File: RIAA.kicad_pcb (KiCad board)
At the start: 2 copper layers, 112 x 202 mm, 44 parts, among them K1 G6K-2, P1 Fra Hovedprint, P2 Fra Ledning, U1 OPA2134, U2 LM317_TO-220

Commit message: feat: reversed D1.
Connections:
- D1 pad 1: 24VDC+ -> 30V
- D1 pad 2: 30V -> 24VDC+
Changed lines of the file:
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@@
 			(layers "*.Cu" "*.Mask")
 			(remove_unused_layers no)
-			(net 14 "24VDC+")
+			(net 15 "30V")
 			(pinfunction "K")
 			(pintype "passive")
@@
 			(layers "*.Cu" "*.Mask")
 			(remove_unused_layers no)
-			(net 15 "30V")
+			(net 14 "24VDC+")
 			(pinfunction "A")
 			(pintype "passive")

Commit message: feat: Updated PSU resistor values.
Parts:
- R1: value 4370 -> 5k6
- R2: value 240 -> 300
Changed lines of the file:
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@@
 			)
 		)
-		(property "Value" "4370"
+		(property "Value" "5k6"
 			(at 3.81 1.92 0)
 			(layer "F.Fab")
@@
 			)
 		)
-		(property "Value" "240"
+		(property "Value" "300"
 			(at 3.81 1.92 0)
 			(layer "F.Fab")

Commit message: feat: Updated PCB.
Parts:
- moved C6 83.7 mm to (165.0, 110.7)
- moved U2 68.7 mm to (150.3, 127.0), turned to -90 degrees
- moved R2 66.8 mm to (183.4, 105.4), turned to 180 degrees
- moved R1 60.3 mm to (163.7, 120.8)
- moved R7 58.7 mm to (239.4, 187.3), turned to 180 degrees
- moved R8 54.4 mm to (231.8, 190.5)
- moved R4 53.3 mm to (231.8, 173.4)
- moved C9 52.5 mm to (180.9, 143.4), turned to 90 degrees
- moved C4 51.9 mm to (218.2, 130.3)
- moved R6 50.6 mm to (231.8, 179.7)
- moved R5 50.6 mm to (231.8, 176.5)
- moved C3 48.9 mm to (149.3, 111.1)
- moved D2 47.5 mm to (188.4, 111.0), turned to 180 degrees
- moved D1 46.1 mm to (173.2, 134.6), turned to 90 degrees
- moved R11 37.1 mm to (205.3, 168.2), turned to 180 degrees
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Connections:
- R11 pad 2: Net-(R11-Pad2) -> GND
- R13 pad 2: Net-(R11-Pad2) -> GND
- R3 pad 2: Net-(R3-Pad2) -> GND
- R5 pad 2: Net-(R3-Pad2) -> GND
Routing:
- net 24VDC+: track 0.00 -> 151.4 mm
- net 24VDC-: track 0.00 -> 54.6 mm
- net 30V: track 7.53 -> 58.6 mm
- net Net-(D2-A): track 0.00 -> 46.1 mm
- net Net-(C11-Pad1): track 0.00 -> 25.2 mm
- net Net-(C16-Pad1): track 0.00 -> 25.1 mm
- net Net-(C10-Pad1): track 0.00 -> 16.7 mm
- net Net-(C15-Pad1): track 0.00 -> 15.9 mm
- net GND: track 78.3 -> 90.4 mm
- net Net-(C15-Pad2): track 0.00 -> 10.7 mm
- net Net-(U3B-+): track 0.00 -> 9.72 mm
- net Net-(U3A-+): track 0.00 -> 8.94 mm
- net Net-(C10-Pad2): track 0.00 -> 8.87 mm
- net R IN  PICKUP: track 0.00 -> 5.52 mm
- net L IN  PICKUP: track 0.00 -> 5.05 mm
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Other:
- board text removed: "PSU"

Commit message: WIP
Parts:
- removed U1: OPA2134, Package_SO:SOIC-8_3.9x4.9mm_P1.27mm
- added U3: OPA2134, OPA2134:D8, F.Cu at (199.0, 181.0)
- moved C10 21.5 mm to (219.9, 189.0)
- moved C11 21.5 mm to (211.0, 189.0)
- moved C12 21.5 mm to (213.6, 199.8)
- moved C16 21.5 mm to (184.9, 187.5)
- moved R15 21.5 mm to (177.0, 191.9)
- moved R3 21.5 mm to (211.0, 175.7)
- moved R4 21.5 mm to (211.0, 178.9)
- moved R5 21.5 mm to (211.0, 182.1)
- moved R7 21.5 mm to (218.6, 192.8)
- moved R8 21.5 mm to (211.0, 196.0)
- moved C15 21.5 mm to (175.8, 187.6)
- moved C17 21.5 mm to (182.0, 200.4)
- moved C8 21.5 mm to (216.1, 171.3)
- moved R6 21.5 mm to (211.0, 185.2)
- moved C14 21.5 mm to (179.7, 169.6)
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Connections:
- BC1 pad 3: 24VDC- -> GND
- C14 pad 2: L IN  PICKUP -> L IN PICKUP
- C3 pad 2: 24VDC- -> GND
- C4 pad 1: 24VDC- -> Net-(U3C-V-)
- C5 pad 2: 24VDC- -> Net-(U3C-V-)
- C6 pad 2: 24VDC- -> GND
- C7 pad 2: 24VDC- -> GND
- C8 pad 2: R IN  PICKUP -> R IN PICKUP
- C9 pad 1: 24VDC- -> GND
- P1 pad 2: 24VDC- -> GND
- P1 pad 3: 24VDC- -> GND
- P2 pad 6: 24VDC- -> GND
- R1 pad 2: 24VDC- -> GND
- R11 pad 1: L IN  PICKUP -> L IN PICKUP
- R3 pad 1: R IN  PICKUP -> R IN PICKUP
- R9 pad 1: 24VDC- -> GND
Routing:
- net 24VDC-: track 54.6 -> 0.00 mm
- net 30V: track 58.6 -> 89.8 mm
- net GND: track 90.4 -> 66.7 mm
- net Net-(BC1-C): track 26.2 -> 40.8 mm, vias 0 -> 2
- net R OUT: track 17.0 -> 5.29 mm
- net 21V: track 45.9 -> 57.0 mm
- net R IN PICKUP: track 0.00 -> 5.52 mm
- net R IN  PICKUP: track 5.52 -> 0.00 mm
- net L IN PICKUP: track 0.00 -> 5.05 mm
- net L IN  PICKUP: track 5.05 -> 0.00 mm
- net L OUT: track 8.73 -> 4.35 mm
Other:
- board text added: "MUTE RELAY"
- board text added: "POWER"
- board text added: "RIAA"

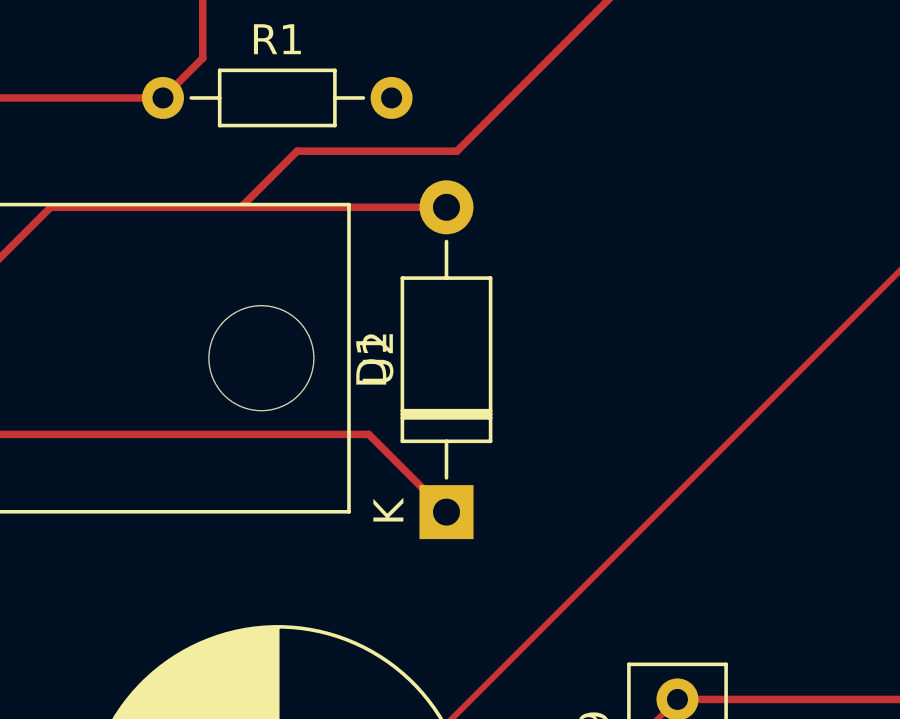
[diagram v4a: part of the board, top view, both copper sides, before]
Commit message: feat: Updated orientation of D1.
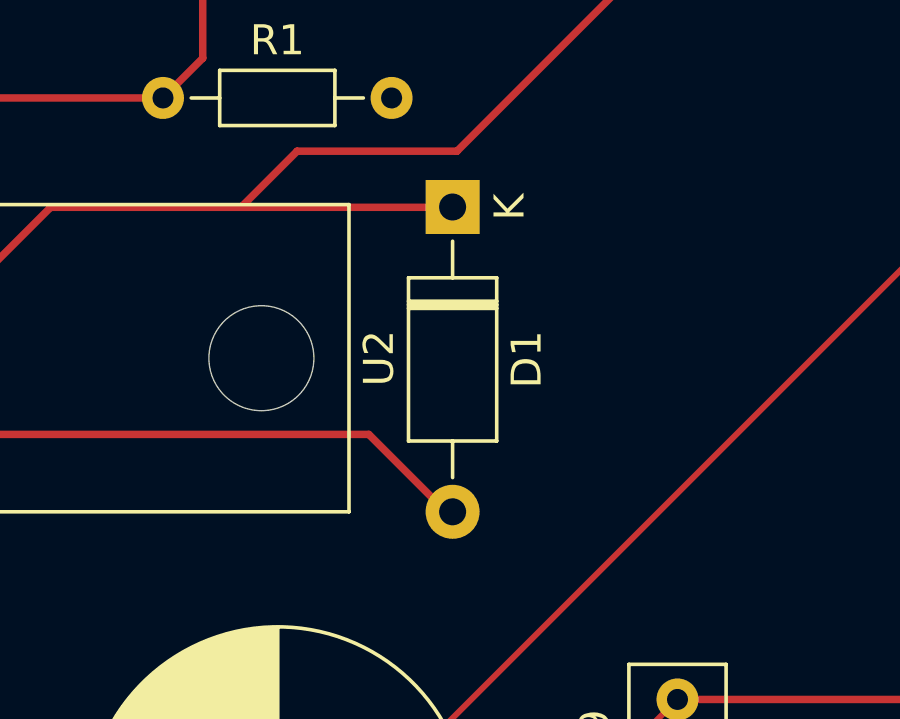
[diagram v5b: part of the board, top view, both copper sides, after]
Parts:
- moved D1 10.2 mm to (173.4, 124.5), turned to -90 degrees
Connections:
- D1 pad 1: 30V -> 24VDC+
- D1 pad 2: 24VDC+ -> 30V
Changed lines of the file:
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@@
 	(footprint "Diode_THT:D_A-405_P10.16mm_Horizontal"
 		(layer "F.Cu")
-		(at 173.151041 134.63 90)
+		(at 173.355 124.46 -90)
 		(descr "Diode, A-405 series, Axial, Horizontal, pin pitch=10.16mm, , length*diameter=5.2*2.7mm^2, , http://www.diodes.com/_files/packages/A-405.pdf")
 		(tags "Diode A-405 series Axial Horizontal pin pitch 10.16mm  length 5.2mm diameter 2.7mm")
@@
 		)
 		(property "Footprint" "Diode_THT:D_A-405_P10.16mm_Horizontal"
-			(at 0 0 90)
+			(at 0 0 -90)
 			(unlocked yes)
 			(layer "F.Fab")
@@
 		)
 		(property "Datasheet" ""
-			(at 0 0 90)
+			(at 0 0 -90)
 			(unlocked yes)
 			(layer "F.Fab")
@@
 		)
 		(property "Description" "Zener diode"
-			(at 0 0 90)
+			(at 0 0 -90)
 			(unlocked yes)
 			(layer "F.Fab")
@@
 		(attr through_hole)
 		(fp_line
+			(start 2.36 1.47)
+			(end 7.8 1.47)
+			(stroke
+				(width 0.12)
+				(type solid)
+			)
+			(layer "F.SilkS")
+		)
+		(fp_line
+			(start 7.8 1.47)
+			(end 7.8 -1.47)
+			(stroke
+				(width 0.12)
+				(type solid)
+			)
+			(layer "F.SilkS")
+		)
+		(fp_line
+			(start 1.14 0)
+			(end 2.36 0)
+			(stroke
+				(width 0.12)
+				(type solid)
+			)
+			(layer "F.SilkS")
+		)
+		(fp_line
+			(start 9.02 0)
+			(end 7.8 0)
+			(stroke
+				(width 0.12)
+				(type solid)
+			)
+			(layer "F.SilkS")
+		)
+		(fp_line
+			(start 2.36 -1.47)
+			(end 2.36 1.47)
+			(stroke
+				(width 0.12)
+				(type solid)
+			)
+			(layer "F.SilkS")
+		)
+		(fp_line
+			(start 3.14 -1.47)
+			(end 3.14 1.47)
+			(stroke
+				(width 0.12)
+				(type solid)
+			)
+			(layer "F.SilkS")
+		)
+		(fp_line
+			(start 3.26 -1.47)
+			(end 3.26 1.47)
+			(stroke
+				(width 0.12)
+				(type solid)
+			)
+			(layer "F.SilkS")
+		)
+		(fp_line
+			(start 3.38 -1.47)
+			(end 3.38 1.47)
+			(stroke
+				(width 0.12)
+				(type solid)
+			)
+			(layer "F.SilkS")
+		)
+		(fp_line
 			(start 7.8 -1.47)
 			(end 2.36 -1.47)
@@
 		)
 		(fp_line
-			(start 3.38 -1.47)
-			(end 3.38 1.47)
-			(stroke
-				(width 0.12)
-				(type solid)
-			)
-			(layer "F.SilkS")
-		)
-		(fp_line
-			(start 3.26 -1.47)
-			(end 3.26 1.47)
-			(stroke
-				(width 0.12)
-				(type solid)
-			)
-			(layer "F.SilkS")
-		)
-		(fp_line
-			(start 3.14 -1.47)
-			(end 3.14 1.47)
-			(stroke
-				(width 0.12)
-				(type solid)
-			)
-			(layer "F.SilkS")
-		)
-		(fp_line
-			(start 2.36 -1.47)
-			(end 2.36 1.47)
-			(stroke
-				(width 0.12)
-				(type solid)
-			)
-			(layer "F.SilkS")
-		)
-		(fp_line
-			(start 9.02 0)
-			(end 7.8 0)
-			(stroke
-				(width 0.12)
-				(type solid)
-			)
-			(layer "F.SilkS")
-		)
-		(fp_line
-			(start 1.14 0)
-			(end 2.36 0)
-			(stroke
-				(width 0.12)
-				(type solid)
-			)
-			(layer "F.SilkS")
-		)
-		(fp_line
-			(start 7.8 1.47)
-			(end 7.8 -1.47)
-			(stroke
-				(width 0.12)
-				(type solid)
-			)
-			(layer "F.SilkS")
-		)
-		(fp_line
-			(start 2.36 1.47)
-			(end 7.8 1.47)
-			(stroke
-				(width 0.12)
-				(type solid)
-			)
-			(layer "F.SilkS")
+			(start -1.15 1.6)
+			(end 11.31 1.6)
+			(stroke
+				(width 0.05)
+				(type solid)
+			)
+			(layer "F.CrtYd")
+		)
+		(fp_line
+			(start 11.31 1.6)
+			(end 11.31 -1.6)
+			(stroke
+				(width 0.05)
+				(type solid)
+			)
+			(layer "F.CrtYd")
+		)
+		(fp_line
+			(start -1.15 -1.6)
+			(end -1.15 1.6)
+			(stroke
+				(width 0.05)
+				(type solid)
+			)
+			(layer "F.CrtYd")
 		)
 		(fp_line
@@
 		)
 		(fp_line
-			(start -1.15 -1.6)
-			(end -1.15 1.6)
-			(stroke
-				(width 0.05)
-				(type solid)
-			)
-			(layer "F.CrtYd")
-		)
-		(fp_line
-			(start 11.31 1.6)
-			(end 11.31 -1.6)
-			(stroke
-				(width 0.05)
-				(type solid)
-			)
-			(layer "F.CrtYd")
-		)
-		(fp_line
-			(start -1.15 1.6)
-			(end 11.31 1.6)
-			(stroke
-				(width 0.05)
-				(type solid)
-			)
-			(layer "F.CrtYd")
+			(start 2.48 1.35)
+			(end 7.68 1.35)
+			(stroke
+				(width 0.1)
+				(type solid)
+			)
+			(layer "F.Fab")
+		)
+		(fp_line
+			(start 7.68 1.35)
+			(end 7.68 -1.35)
+			(stroke
+				(width 0.1)
+				(type solid)
+			)
+			(layer "F.Fab")
+		)
+		(fp_line
+			(start 0 0)
+			(end 2.48 0)
+			(stroke
+				(width 0.1)
+				(type solid)
+			)
+			(layer "F.Fab")
+		)
+		(fp_line
+			(start 10.16 0)
+			(end 7.68 0)
+			(stroke
+				(width 0.1)
+				(type solid)
+			)
+			(layer "F.Fab")
+		)
+		(fp_line
+			(start 2.48 -1.35)
+			(end 2.48 1.35)
+			(stroke
+				(width 0.1)
+				(type solid)
+			)
+			(layer "F.Fab")
+		)
+		(fp_line
+			(start 3.16 -1.35)
+			(end 3.16 1.35)
+			(stroke
+				(width 0.1)
+				(type solid)
+			)
+			(layer "F.Fab")
+		)
+		(fp_line
+			(start 3.26 -1.35)
+			(end 3.26 1.35)
+			(stroke
+				(width 0.1)
+				(type solid)
+			)
+			(layer "F.Fab")
+		)
+		(fp_line
+			(start 3.36 -1.35)
+			(end 3.36 1.35)
+			(stroke
+				(width 0.1)
+				(type solid)
+			)
+			(layer "F.Fab")
 		)
 		(fp_line
@@
 			(layer "F.Fab")
 		)
-		(fp_line
-			(start 3.36 -1.35)
-			(end 3.36 1.35)
-			(stroke
-				(width 0.1)
-				(type solid)
-			)
-			(layer "F.Fab")
-		)
-		(fp_line
-			(start 3.26 -1.35)
-			(end 3.26 1.35)
-			(stroke
-				(width 0.1)
-				(type solid)
-			)
-			(layer "F.Fab")
-		)
-		(fp_line
-			(start 3.16 -1.35)
-			(end 3.16 1.35)
-			(stroke
-				(width 0.1)
-				(type solid)
-			)
-			(layer "F.Fab")
-		)
-		(fp_line
-			(start 2.48 -1.35)
-			(end 2.48 1.35)
-			(stroke
-				(width 0.1)
-				(type solid)
-			)
-			(layer "F.Fab")
-		)
-		(fp_line
-			(start 10.16 0)
-			(end 7.68 0)
-			(stroke
-				(width 0.1)
-				(type solid)
-			)
-			(layer "F.Fab")
-		)
-		(fp_line
-			(start 0 0)
-			(end 2.48 0)
-			(stroke
-				(width 0.1)
-				(type solid)
-			)
-			(layer "F.Fab")
-		)
-		(fp_line
-			(start 7.68 1.35)
-			(end 7.68 -1.35)
-			(stroke
-				(width 0.1)
-				(type solid)
-			)
-			(layer "F.Fab")
-		)
-		(fp_line
-			(start 2.48 1.35)
-			(end 7.68 1.35)
-			(stroke
-				(width 0.1)
-				(type solid)
-			)
-			(layer "F.Fab")
-		)
 		(fp_text user "K"
 			(at 0 -1.9 90)
@@
 		)
 		(pad "1" thru_hole rect
-			(at 0 0 90)
+			(at 0 0 270)
+			(size 1.8 1.8)
+			(drill 0.9)
+			(layers "*.Cu" "*.Mask")
+			(remove_unused_layers no)
+			(net 13 "24VDC+")
+			(pinfunction "K")
+			(pintype "passive")
+		)
+		(pad "2" thru_hole oval
+			(at 10.16 0 270)
 			(size 1.8 1.8)
 			(drill 0.9)
@@
 			(remove_unused_layers no)
 			(net 14 "30V")
-			(pinfunction "K")
-			(pintype "passive")
-		)
-		(pad "2" thru_hole oval
-			(at 10.16 0 90)
-			(size 1.8 1.8)
-			(drill 0.9)
-			(layers "*.Cu" "*.Mask")
-			(remove_unused_layers no)
-			(net 13 "24VDC+")
 			(pinfunction "A")
 			(pintype "passive")

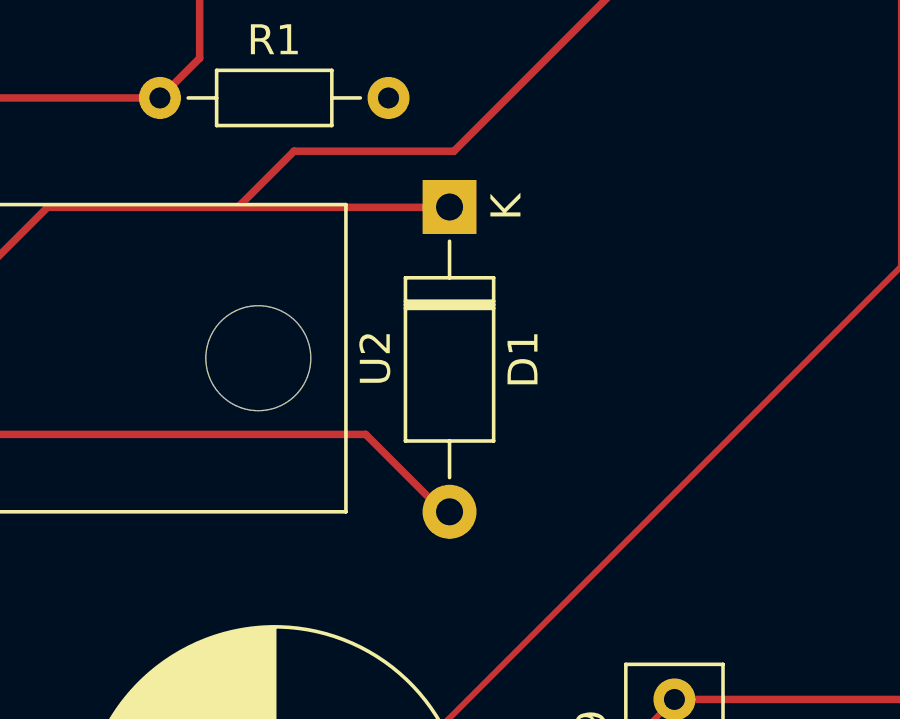
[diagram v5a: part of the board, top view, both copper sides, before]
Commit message: feat: Updated orientation of D1.
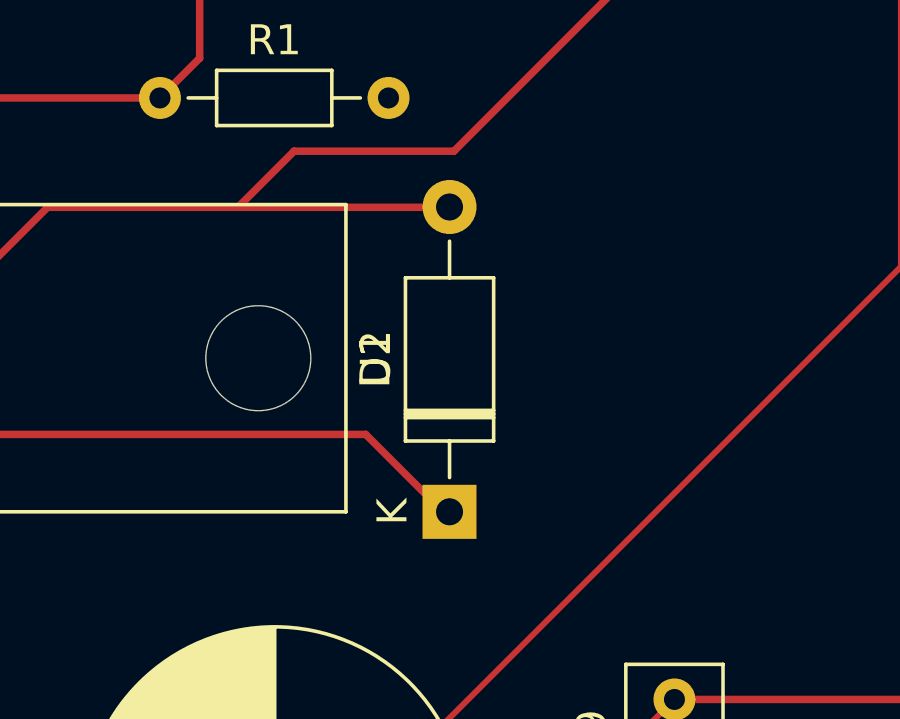
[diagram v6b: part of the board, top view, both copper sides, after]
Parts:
- moved D1 10.2 mm to (173.4, 134.6), turned to 90 degrees
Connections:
- D1 pad 1: 24VDC+ -> 30V
- D1 pad 2: 30V -> 24VDC+
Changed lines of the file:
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@@
 	(footprint "Diode_THT:D_A-405_P10.16mm_Horizontal"
 		(layer "F.Cu")
-		(at 173.355 124.46 -90)
+		(at 173.355 134.62 90)
 		(descr "Diode, A-405 series, Axial, Horizontal, pin pitch=10.16mm, , length*diameter=5.2*2.7mm^2, , http://www.diodes.com/_files/packages/A-405.pdf")
 		(tags "Diode A-405 series Axial Horizontal pin pitch 10.16mm  length 5.2mm diameter 2.7mm")
@@
 		)
 		(property "Footprint" "Diode_THT:D_A-405_P10.16mm_Horizontal"
-			(at 0 0 -90)
+			(at 0 0 90)
 			(unlocked yes)
 			(layer "F.Fab")
@@
 		)
 		(property "Datasheet" ""
-			(at 0 0 -90)
+			(at 0 0 90)
 			(unlocked yes)
 			(layer "F.Fab")
@@
 		)
 		(property "Description" "Zener diode"
-			(at 0 0 -90)
+			(at 0 0 90)
 			(unlocked yes)
 			(layer "F.Fab")
@@
 		(attr through_hole)
 		(fp_line
+			(start 7.8 -1.47)
+			(end 2.36 -1.47)
+			(stroke
+				(width 0.12)
+				(type solid)
+			)
+			(layer "F.SilkS")
+		)
+		(fp_line
+			(start 3.38 -1.47)
+			(end 3.38 1.47)
+			(stroke
+				(width 0.12)
+				(type solid)
+			)
+			(layer "F.SilkS")
+		)
+		(fp_line
+			(start 3.26 -1.47)
+			(end 3.26 1.47)
+			(stroke
+				(width 0.12)
+				(type solid)
+			)
+			(layer "F.SilkS")
+		)
+		(fp_line
+			(start 3.14 -1.47)
+			(end 3.14 1.47)
+			(stroke
+				(width 0.12)
+				(type solid)
+			)
+			(layer "F.SilkS")
+		)
+		(fp_line
+			(start 2.36 -1.47)
+			(end 2.36 1.47)
+			(stroke
+				(width 0.12)
+				(type solid)
+			)
+			(layer "F.SilkS")
+		)
+		(fp_line
+			(start 9.02 0)
+			(end 7.8 0)
+			(stroke
+				(width 0.12)
+				(type solid)
+			)
+			(layer "F.SilkS")
+		)
+		(fp_line
+			(start 1.14 0)
+			(end 2.36 0)
+			(stroke
+				(width 0.12)
+				(type solid)
+			)
+			(layer "F.SilkS")
+		)
+		(fp_line
+			(start 7.8 1.47)
+			(end 7.8 -1.47)
+			(stroke
+				(width 0.12)
+				(type solid)
+			)
+			(layer "F.SilkS")
+		)
+		(fp_line
 			(start 2.36 1.47)
 			(end 7.8 1.47)
@@
 		)
 		(fp_line
-			(start 7.8 1.47)
-			(end 7.8 -1.47)
-			(stroke
-				(width 0.12)
-				(type solid)
-			)
-			(layer "F.SilkS")
-		)
-		(fp_line
-			(start 1.14 0)
-			(end 2.36 0)
-			(stroke
-				(width 0.12)
-				(type solid)
-			)
-			(layer "F.SilkS")
-		)
-		(fp_line
-			(start 9.02 0)
-			(end 7.8 0)
-			(stroke
-				(width 0.12)
-				(type solid)
-			)
-			(layer "F.SilkS")
-		)
-		(fp_line
-			(start 2.36 -1.47)
-			(end 2.36 1.47)
-			(stroke
-				(width 0.12)
-				(type solid)
-			)
-			(layer "F.SilkS")
-		)
-		(fp_line
-			(start 3.14 -1.47)
-			(end 3.14 1.47)
-			(stroke
-				(width 0.12)
-				(type solid)
-			)
-			(layer "F.SilkS")
-		)
-		(fp_line
-			(start 3.26 -1.47)
-			(end 3.26 1.47)
-			(stroke
-				(width 0.12)
-				(type solid)
-			)
-			(layer "F.SilkS")
-		)
-		(fp_line
-			(start 3.38 -1.47)
-			(end 3.38 1.47)
-			(stroke
-				(width 0.12)
-				(type solid)
-			)
-			(layer "F.SilkS")
-		)
-		(fp_line
-			(start 7.8 -1.47)
-			(end 2.36 -1.47)
-			(stroke
-				(width 0.12)
-				(type solid)
-			)
-			(layer "F.SilkS")
+			(start 11.31 -1.6)
+			(end -1.15 -1.6)
+			(stroke
+				(width 0.05)
+				(type solid)
+			)
+			(layer "F.CrtYd")
+		)
+		(fp_line
+			(start -1.15 -1.6)
+			(end -1.15 1.6)
+			(stroke
+				(width 0.05)
+				(type solid)
+			)
+			(layer "F.CrtYd")
+		)
+		(fp_line
+			(start 11.31 1.6)
+			(end 11.31 -1.6)
+			(stroke
+				(width 0.05)
+				(type solid)
+			)
+			(layer "F.CrtYd")
 		)
 		(fp_line
@@
 		)
 		(fp_line
-			(start 11.31 1.6)
-			(end 11.31 -1.6)
-			(stroke
-				(width 0.05)
-				(type solid)
-			)
-			(layer "F.CrtYd")
-		)
-		(fp_line
-			(start -1.15 -1.6)
-			(end -1.15 1.6)
-			(stroke
-				(width 0.05)
-				(type solid)
-			)
-			(layer "F.CrtYd")
-		)
-		(fp_line
-			(start 11.31 -1.6)
-			(end -1.15 -1.6)
-			(stroke
-				(width 0.05)
-				(type solid)
-			)
-			(layer "F.CrtYd")
+			(start 7.68 -1.35)
+			(end 2.48 -1.35)
+			(stroke
+				(width 0.1)
+				(type solid)
+			)
+			(layer "F.Fab")
+		)
+		(fp_line
+			(start 3.36 -1.35)
+			(end 3.36 1.35)
+			(stroke
+				(width 0.1)
+				(type solid)
+			)
+			(layer "F.Fab")
+		)
+		(fp_line
+			(start 3.26 -1.35)
+			(end 3.26 1.35)
+			(stroke
+				(width 0.1)
+				(type solid)
+			)
+			(layer "F.Fab")
+		)
+		(fp_line
+			(start 3.16 -1.35)
+			(end 3.16 1.35)
+			(stroke
+				(width 0.1)
+				(type solid)
+			)
+			(layer "F.Fab")
+		)
+		(fp_line
+			(start 2.48 -1.35)
+			(end 2.48 1.35)
+			(stroke
+				(width 0.1)
+				(type solid)
+			)
+			(layer "F.Fab")
+		)
+		(fp_line
+			(start 10.16 0)
+			(end 7.68 0)
+			(stroke
+				(width 0.1)
+				(type solid)
+			)
+			(layer "F.Fab")
+		)
+		(fp_line
+			(start 0 0)
+			(end 2.48 0)
+			(stroke
+				(width 0.1)
+				(type solid)
+			)
+			(layer "F.Fab")
+		)
+		(fp_line
+			(start 7.68 1.35)
+			(end 7.68 -1.35)
+			(stroke
+				(width 0.1)
+				(type solid)
+			)
+			(layer "F.Fab")
 		)
 		(fp_line
@@
 			(layer "F.Fab")
 		)
-		(fp_line
-			(start 7.68 1.35)
-			(end 7.68 -1.35)
-			(stroke
-				(width 0.1)
-				(type solid)
-			)
-			(layer "F.Fab")
-		)
-		(fp_line
-			(start 0 0)
-			(end 2.48 0)
-			(stroke
-				(width 0.1)
-				(type solid)
-			)
-			(layer "F.Fab")
-		)
-		(fp_line
-			(start 10.16 0)
-			(end 7.68 0)
-			(stroke
-				(width 0.1)
-				(type solid)
-			)
-			(layer "F.Fab")
-		)
-		(fp_line
-			(start 2.48 -1.35)
-			(end 2.48 1.35)
-			(stroke
-				(width 0.1)
-				(type solid)
-			)
-			(layer "F.Fab")
-		)
-		(fp_line
-			(start 3.16 -1.35)
-			(end 3.16 1.35)
-			(stroke
-				(width 0.1)
-				(type solid)
-			)
-			(layer "F.Fab")
-		)
-		(fp_line
-			(start 3.26 -1.35)
-			(end 3.26 1.35)
-			(stroke
-				(width 0.1)
-				(type solid)
-			)
-			(layer "F.Fab")
-		)
-		(fp_line
-			(start 3.36 -1.35)
-			(end 3.36 1.35)
-			(stroke
-				(width 0.1)
-				(type solid)
-			)
-			(layer "F.Fab")
-		)
-		(fp_line
-			(start 7.68 -1.35)
-			(end 2.48 -1.35)
-			(stroke
-				(width 0.1)
-				(type solid)
-			)
-			(layer "F.Fab")
-		)
 		(fp_text user "K"
 			(at 0 -1.9 90)
@@
 		)
 		(pad "1" thru_hole rect
-			(at 0 0 270)
+			(at 0 0 90)
+			(size 1.8 1.8)
+			(drill 0.9)
+			(layers "*.Cu" "*.Mask")
+			(remove_unused_layers no)
+			(net 14 "30V")
+			(pinfunction "K")
+			(pintype "passive")
+		)
+		(pad "2" thru_hole oval
+			(at 10.16 0 90)
 			(size 1.8 1.8)
 			(drill 0.9)
@@
 			(remove_unused_layers no)
 			(net 13 "24VDC+")
-			(pinfunction "K")
-			(pintype "passive")
-		)
-		(pad "2" thru_hole oval
-			(at 10.16 0 270)
-			(size 1.8 1.8)
-			(drill 0.9)
-			(layers "*.Cu" "*.Mask")
-			(remove_unused_layers no)
-			(net 14 "30V")
 			(pinfunction "A")
 			(pintype "passive")
